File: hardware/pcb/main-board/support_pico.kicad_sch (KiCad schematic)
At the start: 27 parts, among them J701 Conn_01x02, J702 Z88 SD Card, U702 RP2040, U703 W25Q128JVS, Y701 ABLS-12.000MHZ-B4-T

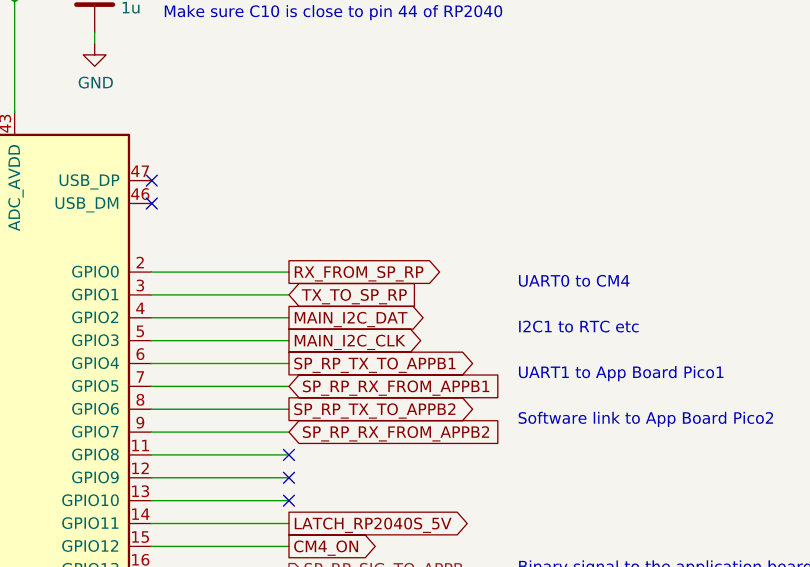
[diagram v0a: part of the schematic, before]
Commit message: rename CM4 to support RP link
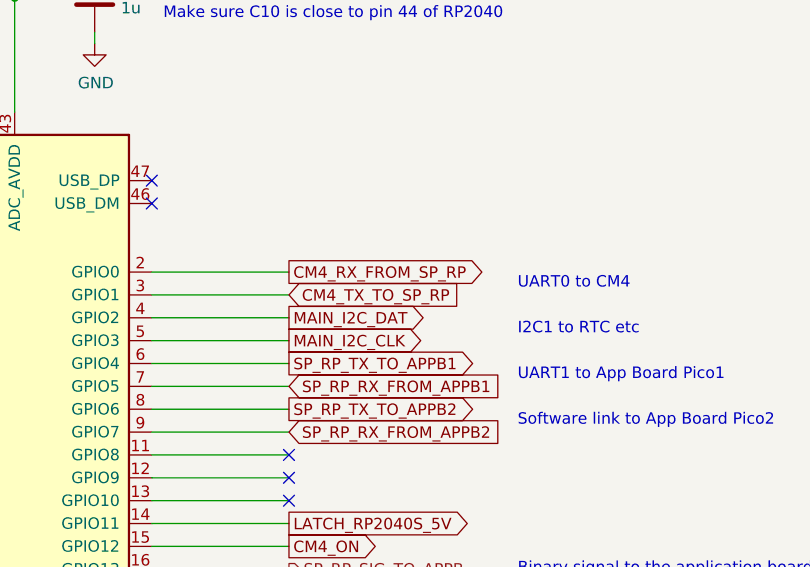
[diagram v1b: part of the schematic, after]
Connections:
- net RX_FROM_SP_RP: no longer U702.2 (GPIO0)
- net TX_TO_SP_RP: no longer U702.3 (GPIO1)
- new net CM4_RX_FROM_SP_RP: U702.2 (GPIO0)
- new net CM4_TX_TO_SP_RP: U702.3 (GPIO1)
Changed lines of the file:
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@@
 		)
 	)
-	(global_label "RX_FROM_SP_RP"
+	(global_label "CM4_RX_FROM_SP_RP"
 		(shape output)
 		(at 113.03 71.12 0)
@@
 		)
 		(property "Intersheetrefs" "${INTERSHEET_REFS}"
-			(at 130.9033 71.12 0)
+			(at 135.8018 71.12 0)
 			(effects
 				(font
@@
 		)
 	)
-	(global_label "TX_TO_SP_RP"
+	(global_label "CM4_TX_TO_SP_RP"
 		(shape input)
 		(at 113.03 73.66 0)
@@
 		)
 		(property "Intersheetrefs" "${INTERSHEET_REFS}"
-			(at 127.7585 73.66 0)
+			(at 132.657 73.66 0)
 			(effects
 				(font
